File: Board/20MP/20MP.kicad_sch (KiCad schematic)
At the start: 48 parts, among them J1 Conn_01x02_Male, SW1 SHOU_HAN_MSK12C02-HB, SW2 RotaryEncoder_Switch, U1 nice_nanoV2

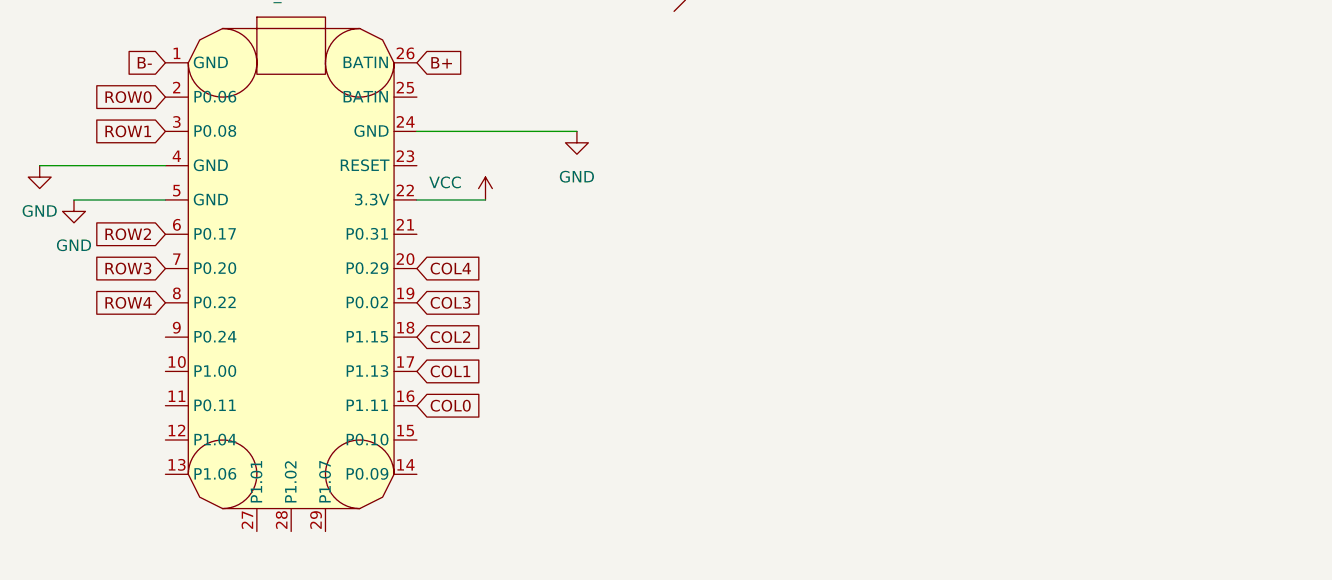
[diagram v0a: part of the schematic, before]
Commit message: added nice view to shematic
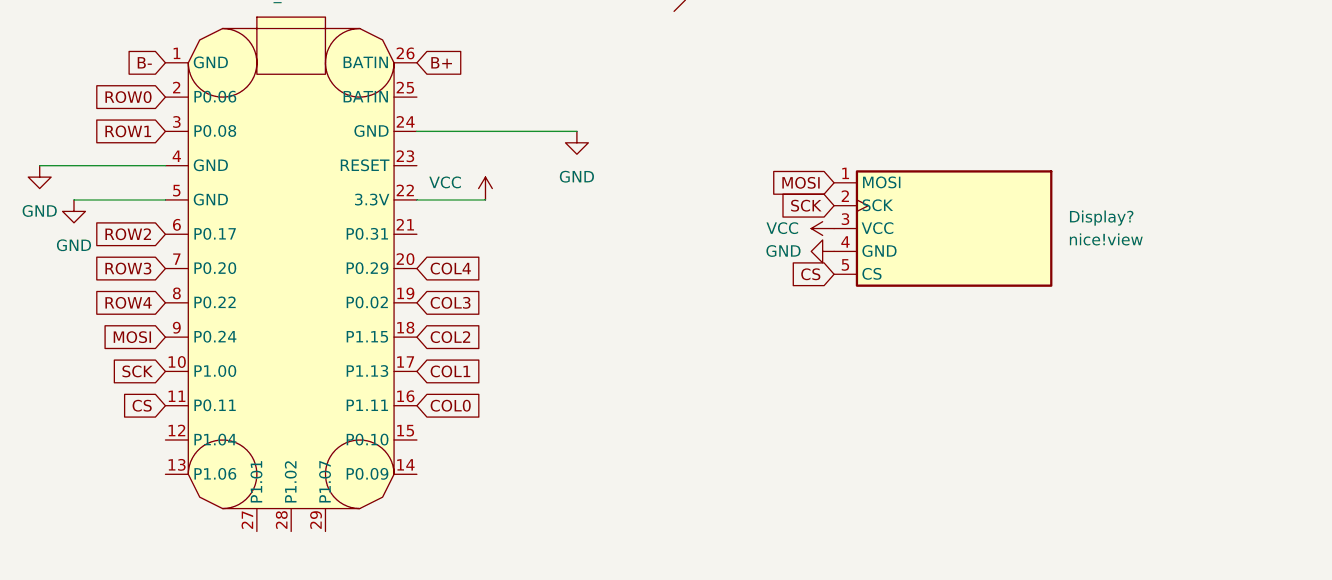
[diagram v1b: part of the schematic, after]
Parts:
- added Display?: nice!view, nice_view:nice_view, symbol microcontroller:nice!view
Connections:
- net GND: now also Display?.4 (GND)
- net VCC: now also Display?.3 (VCC)
- net SCK: now reaches U1.10 (P1.00)
- net SCK: now also Display?.2 (SCK)
- net CS: now reaches U1.11 (P0.11)
- net CS: now also Display?.5 (CS)
- net MOSI: now reaches U1.9 (P0.24)
- net MOSI: now also Display?.1 (MOSI)
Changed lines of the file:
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@@
+    )
+  )
+  (global_label "CS" (shape input) (at 63.5 105.41 180) (fields_autoplaced)
+    (effects (font (size 1.27 1.27)) (justify right))
+    (property "Intersheet References" "${INTERSHEET_REFS}" (id 0) (at 58.6074 105.3306 0)
+      (effects (font (size 1.27 1.27)) (justify right) hide)
+    )
+  )
+  (global_label "SCK" (shape input) (at 137.795 83.185 180) (fields_autoplaced)
+    (effects (font (size 1.27 1.27)) (justify right))
+    (property "Intersheet References" "${INTERSHEET_REFS}" (id 0) (at 131.6324 83.1056 0)
+      (effects (font (size 1.27 1.27)) (justify right) hide)
+    )
+  )
+  (global_label "SCK" (shape input) (at 63.5 101.6 180) (fields_autoplaced)
+    (effects (font (size 1.27 1.27)) (justify right))
+    (property "Intersheet References" "${INTERSHEET_REFS}" (id 0) (at 57.3374 101.5206 0)
+      (effects (font (size 1.27 1.27)) (justify right) hide)
     )
   )
@@
     )
   )
+  (global_label "MOSI" (shape input) (at 63.5 97.79 180) (fields_autoplaced)
+    (effects (font (size 1.27 1.27)) (justify right))
+    (property "Intersheet References" "${INTERSHEET_REFS}" (id 0) (at 56.4907 97.7106 0)
+      (effects (font (size 1.27 1.27)) (justify right) hide)
+    )
+  )
+  (global_label "MOSI" (shape input) (at 137.795 80.645 180) (fields_autoplaced)
+    (effects (font (size 1.27 1.27)) (justify right))
+    (property "Intersheet References" "${INTERSHEET_REFS}" (id 0) (at 130.7857 80.5656 0)
+      (effects (font (size 1.27 1.27)) (justify right) hide)
+    )
+  )
   (global_label "B+" (shape input) (at 112.395 52.705 180) (fields_autoplaced)
     (effects (font (size 1.27 1.27)) (justify right))
@@
     )
   )
+  (global_label "CS" (shape input) (at 137.795 90.805 180) (fields_autoplaced)
+    (effects (font (size 1.27 1.27)) (justify right))
+    (property "Intersheet References" "${INTERSHEET_REFS}" (id 0) (at 132.9024 90.7256 0)
+      (effects (font (size 1.27 1.27)) (justify right) hide)
+    )
+  )
   (global_label "B+" (shape input) (at 91.44 67.31 0) (fields_autoplaced)
     (effects (font (size 1.27 1.27)) (justify left))
@@
     (pin "1")
     (pin "2")
+  )
+  (symbol (lib_id "power:GND") (at 137.795 88.265 270) (unit 1)
+    (in_bom yes) (on_board yes)
+    (property "Reference" "#PWR?" (id 0) (at 131.445 88.265 0)
+      (effects (font (size 1.27 1.27)) hide)
+    )
+    (property "Value" "GND" (id 1) (at 130.175 88.265 90)
+      (effects (font (size 1.27 1.27)) (justify left))
+    )
+    (property "Footprint" "" (id 2) (at 137.795 88.265 0)
+      (effects (font (size 1.27 1.27)) hide)
+    )
+    (property "Datasheet" "" (id 3) (at 137.795 88.265 0)
+      (effects (font (size 1.27 1.27)) hide)
+    )
+    (pin "1")
   )
   (symbol (lib_id "led:D_Small") (at 267.335 151.765 90) (unit 1)
@@
     (pin "1")
     (pin "2")
+  )
+  (symbol (lib_id "power:VCC") (at 137.795 85.725 90) (unit 1)
+    (in_bom yes) (on_board yes)
+    (property "Reference" "#PWR?" (id 0) (at 141.605 85.725 0)
+      (effects (font (size 1.27 1.27)) hide)
+    )
+    (property "Value" "VCC" (id 1) (at 132.08 85.725 90))
+    (property "Footprint" "" (id 2) (at 137.795 85.725 0)
+      (effects (font (size 1.27 1.27)) hide)
+    )
+    (property "Datasheet" "" (id 3) (at 137.795 85.725 0)
+      (effects (font (size 1.27 1.27)) hide)
+    )
+    (pin "1")
   )
   (symbol (lib_id "pcb-rescue:MX-NoLED-MX_Alps_Hybrid") (at 220.345 145.415 0) (unit 1)
@@
     (pin "2")
   )
+  (symbol (lib_id "microcontroller:nice!view") (at 150.495 85.725 270) (unit 1)
+    (in_bom yes) (on_board yes) (fields_autoplaced)
+    (property "Reference" "Display?" (id 0) (at 163.83 84.4549 90)
+      (effects (font (size 1.27 1.27)) (justify left))
+    )
+    (property "Value" "nice!view" (id 1) (at 163.83 86.9949 90)
+      (effects (font (size 1.27 1.27)) (justify left))
+    )
+    (property "Footprint" "nice_view:nice_view" (id 2) (at 167.005 85.725 0)
+      (effects (font (size 1.27 1.27)) hide)
+    )
+    (property "Datasheet" "https://nicekeyboards.com/docs/nice-view/pinout-schematic" (id 3) (at 125.095 88.265 0)
+      (effects (font (size 1.27 1.27)) hide)
+    )
+    (pin "1")
+    (pin "2")
+    (pin "3")
+    (pin "4")
+    (pin "5")
+  )
   (symbol (lib_id "pcb-rescue:MX-NoLED-MX_Alps_Hybrid") (at 245.745 191.135 0) (unit 1)
     (in_bom yes) (on_board yes)
@@
       (reference "#PWR0107") (unit 1) (value "GND") (footprint "")
     )
+    (path "/077fa9e8-6ace-47c7-b2d9-a10ce67b4b2e"
+      (reference "#PWR?") (unit 1) (value "GND") (footprint "")
+    )
+    (path "/93480eee-d9fe-413d-9b83-523b8639fae5"
+      (reference "#PWR?") (unit 1) (value "VCC") (footprint "")
+    )
     (path "/737fc51a-35ee-45cc-8be4-9d28881bc01a"
       (reference "D1") (unit 1) (value "1.25V@150mA") (footprint "Diode_THT:D_DO-35_SOD27_P7.62mm_Horizontal")
@@
       (reference "D18") (unit 1) (value "1.25V@150mA") (footprint "Diode_THT:D_DO-35_SOD27_P7.62mm_Horizontal")
     )
+    (path "/fa417416-1aaa-4fd6-ba5d-3347f975a221"
+      (reference "Display?") (unit 1) (value "nice!view") (footprint "nice_view:nice_view")
+    )
     (path "/23241be8-f73f-4bb3-84de-fa8fd5f8d281"

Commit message: added nice view
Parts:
- Display1: renamed from Display?; footprint nice_view:nice_view -> microcontroller:nice_view
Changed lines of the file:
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@@
   (symbol (lib_id "power:GND") (at 137.795 88.265 270) (unit 1)
     (in_bom yes) (on_board yes)
-    (property "Reference" "#PWR?" (id 0) (at 131.445 88.265 0)
+    (property "Reference" "#PWR0101" (id 0) (at 131.445 88.265 0)
       (effects (font (size 1.27 1.27)) hide)
     )
@@
   (symbol (lib_id "power:VCC") (at 137.795 85.725 90) (unit 1)
     (in_bom yes) (on_board yes)
-    (property "Reference" "#PWR?" (id 0) (at 141.605 85.725 0)
+    (property "Reference" "#PWR0108" (id 0) (at 141.605 85.725 0)
       (effects (font (size 1.27 1.27)) hide)
     )
@@
   (symbol (lib_id "microcontroller:nice!view") (at 150.495 85.725 270) (unit 1)
     (in_bom yes) (on_board yes) (fields_autoplaced)
-    (property "Reference" "Display?" (id 0) (at 163.83 84.4549 90)
+    (property "Reference" "Display1" (id 0) (at 163.83 84.4549 90)
       (effects (font (size 1.27 1.27)) (justify left))
     )
@@
       (effects (font (size 1.27 1.27)) (justify left))
     )
-    (property "Footprint" "nice_view:nice_view" (id 2) (at 167.005 85.725 0)
+    (property "Footprint" "microcontroller:nice_view" (id 2) (at 167.005 85.725 0)
       (effects (font (size 1.27 1.27)) hide)
     )
@@
   )
   (symbol_instances
+    (path "/077fa9e8-6ace-47c7-b2d9-a10ce67b4b2e"
+      (reference "#PWR0101") (unit 1) (value "GND") (footprint "")
+    )
     (path "/1407de64-f7a0-4a9a-bd83-2447e7e8897c"
       (reference "#PWR0102") (unit 1) (value "GND") (footprint "")
@@
       (reference "#PWR0107") (unit 1) (value "GND") (footprint "")
     )
-    (path "/077fa9e8-6ace-47c7-b2d9-a10ce67b4b2e"
-      (reference "#PWR?") (unit 1) (value "GND") (footprint "")
-    )
     (path "/93480eee-d9fe-413d-9b83-523b8639fae5"
-      (reference "#PWR?") (unit 1) (value "VCC") (footprint "")
+      (reference "#PWR0108") (unit 1) (value "VCC") (footprint "")
     )
     (path "/737fc51a-35ee-45cc-8be4-9d28881bc01a"
@@
     )
     (path "/fa417416-1aaa-4fd6-ba5d-3347f975a221"
-      (reference "Display?") (unit 1) (value "nice!view") (footprint "nice_view:nice_view")
+      (reference "Display1") (unit 1) (value "nice!view") (footprint "microcontroller:nice_view")
     )
     (path "/23241be8-f73f-4bb3-84de-fa8fd5f8d281"

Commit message: changed diodes to smd
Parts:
- D1, D10, D11, D12, D13, D14, D15, D16, D17, D18, D2, D3, D4, D5, D6, D7, D8, D9: footprint Diode_THT:D_DO-35_SOD27_P7.62mm_Horizontal -> led:led_capacitor

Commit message: added matrix traces
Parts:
- D1, D10, D11, D12, D13, D14, D15, D16, D17, D18, D2, D3, D4, D5, D6, D7, D8, D9: footprint led:led_capacitor -> led:D_SOD-123
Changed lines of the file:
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@@
       (effects (font (size 1.27 1.27)) (justify right))
     )
-    (property "Footprint" "led:led_capacitor" (id 2) (at 216.535 187.325 90)
+    (property "Footprint" "led:D_SOD-123" (id 2) (at 216.535 187.325 90)
       (effects (font (size 1.27 1.27)) hide)
     )
@@
       (effects (font (size 1.27 1.27)) (justify right))
     )
-    (property "Footprint" "led:led_capacitor" (id 2) (at 267.335 141.605 90)
+    (property "Footprint" "led:D_SOD-123" (id 2) (at 267.335 141.605 90)
       (effects (font (size 1.27 1.27)) hide)
     )
@@
       (effects (font (size 1.27 1.27)) (justify right))
     )
-    (property "Footprint" "led:led_capacitor" (id 2) (at 216.535 167.005 90)
+    (property "Footprint" "led:D_SOD-123" (id 2) (at 216.535 167.005 90)
       (effects (font (size 1.27 1.27)) hide)
     )
@@
       (effects (font (size 1.27 1.27)) (justify right))
     )
-    (property "Footprint" "led:led_capacitor" (id 2) (at 314.96 177.8 90)
+    (property "Footprint" "led:D_SOD-123" (id 2) (at 314.96 177.8 90)
       (effects (font (size 1.27 1.27)) hide)
     )
@@
       (effects (font (size 1.27 1.27)) (justify right))
     )
-    (property "Footprint" "led:led_capacitor" (id 2) (at 267.335 167.005 90)
+    (property "Footprint" "led:D_SOD-123" (id 2) (at 267.335 167.005 90)
       (effects (font (size 1.27 1.27)) hide)
     )
@@
       (effects (font (size 1.27 1.27)) (justify right))
     )
-    (property "Footprint" "led:led_capacitor" (id 2) (at 267.335 116.205 90)
+    (property "Footprint" "led:D_SOD-123" (id 2) (at 267.335 116.205 90)
       (effects (font (size 1.27 1.27)) hide)
     )
@@
       (effects (font (size 1.27 1.27)) (justify right))
     )
-    (property "Footprint" "led:led_capacitor" (id 2) (at 216.535 141.605 90)
+    (property "Footprint" "led:D_SOD-123" (id 2) (at 216.535 141.605 90)
       (effects (font (size 1.27 1.27)) hide)
     )
@@
       (effects (font (size 1.27 1.27)) (justify right))
     )
-    (property "Footprint" "led:led_capacitor" (id 2) (at 241.935 141.605 90)
+    (property "Footprint" "led:D_SOD-123" (id 2) (at 241.935 141.605 90)
       (effects (font (size 1.27 1.27)) hide)
     )
@@
       (effects (font (size 1.27 1.27)) (justify right))
     )
-    (property "Footprint" "led:led_capacitor" (id 2) (at 216.535 90.805 90)
+    (property "Footprint" "led:D_SOD-123" (id 2) (at 216.535 90.805 90)
       (effects (font (size 1.27 1.27)) hide)
     )
@@
       (effects (font (size 1.27 1.27)) (justify right))
     )
-    (property "Footprint" "led:led_capacitor" (id 2) (at 292.735 116.205 90)
+    (property "Footprint" "led:D_SOD-123" (id 2) (at 292.735 116.205 90)
       (effects (font (size 1.27 1.27)) hide)
     )
@@
       (effects (font (size 1.27 1.27)) (justify right))
     )
-    (property "Footprint" "led:led_capacitor" (id 2) (at 216.535 116.205 90)
+    (property "Footprint" "led:D_SOD-123" (id 2) (at 216.535 116.205 90)
       (effects (font (size 1.27 1.27)) hide)
     )
@@
       (effects (font (size 1.27 1.27)) (justify right))
     )
-    (property "Footprint" "led:led_capacitor" (id 2) (at 241.935 167.005 90)
+    (property "Footprint" "led:D_SOD-123" (id 2) (at 241.935 167.005 90)
       (effects (font (size 1.27 1.27)) hide)
     )
@@
       (effects (font (size 1.27 1.27)) (justify right))
     )
-    (property "Footprint" "led:led_capacitor" (id 2) (at 241.935 90.805 90)
+    (property "Footprint" "led:D_SOD-123" (id 2) (at 241.935 90.805 90)
       (effects (font (size 1.27 1.27)) hide)
     )
@@
       (effects (font (size 1.27 1.27)) (justify right))
     )
-    (property "Footprint" "led:led_capacitor" (id 2) (at 241.935 187.325 90)
+    (property "Footprint" "led:D_SOD-123" (id 2) (at 241.935 187.325 90)
       (effects (font (size 1.27 1.27)) hide)
     )
@@
       (effects (font (size 1.27 1.27)) (justify right))
     )
-    (property "Footprint" "led:led_capacitor" (id 2) (at 292.735 90.805 90)
+    (property "Footprint" "led:D_SOD-123" (id 2) (at 292.735 90.805 90)
       (effects (font (size 1.27 1.27)) hide)
     )
@@
       (effects (font (size 1.27 1.27)) (justify right))
     )
-    (property "Footprint" "led:led_capacitor" (id 2) (at 292.735 141.605 90)
+    (property "Footprint" "led:D_SOD-123" (id 2) (at 292.735 141.605 90)
       (effects (font (size 1.27 1.27)) hide)
     )
@@
       (effects (font (size 1.27 1.27)) (justify right))
     )
-    (property "Footprint" "led:led_capacitor" (id 2) (at 267.335 90.805 90)
+    (property "Footprint" "led:D_SOD-123" (id 2) (at 267.335 90.805 90)
       (effects (font (size 1.27 1.27)) hide)
     )
@@
       (effects (font (size 1.27 1.27)) (justify right))
     )
-    (property "Footprint" "led:led_capacitor" (id 2) (at 241.935 116.205 90)
+    (property "Footprint" "led:D_SOD-123" (id 2) (at 241.935 116.205 90)
       (effects (font (size 1.27 1.27)) hide)
     )
@@
     )
     (path "/737fc51a-35ee-45cc-8be4-9d28881bc01a"
-      (reference "D1") (unit 1) (value "1.25V@150mA") (footprint "led:led_capacitor")
+      (reference "D1") (unit 1) (value "1.25V@150mA") (footprint "led:D_SOD-123")
     )
     (path "/828cf1c3-df22-4977-bdc4-6d4dc39f11a6"
-      (reference "D2") (unit 1) (value "1.25V@150mA") (footprint "led:led_capacitor")
+      (reference "D2") (unit 1) (value "1.25V@150mA") (footprint "led:D_SOD-123")
     )
     (path "/70d2644a-7097-4af7-a972-803c0d643478"
-      (reference "D3") (unit 1) (value "1.25V@150mA") (footprint "led:led_capacitor")
+      (reference "D3") (unit 1) (value "1.25V@150mA") (footprint "led:D_SOD-123")
     )
     (path "/249d342e-814c-4657-b87f-4a948cf09f83"
-      (reference "D4") (unit 1) (value "1.25V@150mA") (footprint "led:led_capacitor")
+      (reference "D4") (unit 1) (value "1.25V@150mA") (footprint "led:D_SOD-123")
     )
     (path "/0142f8b5-c800-43db-9d31-5f9eb56a3541"
-      (reference "D5") (unit 1) (value "1.25V@150mA") (footprint "led:led_capacitor")
+      (reference "D5") (unit 1) (value "1.25V@150mA") (footprint "led:D_SOD-123")
     )
     (path "/ba13f5a9-b55a-43bb-9158-6065ece3054a"
-      (reference "D6") (unit 1) (value "1.25V@150mA") (footprint "led:led_capacitor")
+      (reference "D6") (unit 1) (value "1.25V@150mA") (footprint "led:D_SOD-123")
     )
     (path "/f52a7792-b2ba-41b3-b87f-915a0d15a464"
-      (reference "D7") (unit 1) (value "1.25V@150mA") (footprint "led:led_capacitor")
+      (reference "D7") (unit 1) (value "1.25V@150mA") (footprint "led:D_SOD-123")
     )
     (path "/733cc8ef-d71d-4b0e-b748-90c3ff173b3e"
-      (reference "D8") (unit 1) (value "1.25V@150mA") (footprint "led:led_capacitor")
+      (reference "D8") (unit 1) (value "1.25V@150mA") (footprint "led:D_SOD-123")
     )
     (path "/ac5ab474-27f7-4252-9f2e-0a1481cf7f98"
-      (reference "D9") (unit 1) (value "1.25V@150mA") (footprint "led:led_capacitor")
+      (reference "D9") (unit 1) (value "1.25V@150mA") (footprint "led:D_SOD-123")
     )
     (path "/c14c0489-ba57-4809-b1ce-5b757b133c92"
-      (reference "D10") (unit 1) (value "1.25V@150mA") (footprint "led:led_capacitor")
+      (reference "D10") (unit 1) (value "1.25V@150mA") (footprint "led:D_SOD-123")
     )
     (path "/ee591613-253d-445b-b2ba-194a6782e1b3"
-      (reference "D11") (unit 1) (value "1.25V@150mA") (footprint "led:led_capacitor")
+      (reference "D11") (unit 1) (value "1.25V@150mA") (footprint "led:D_SOD-123")
     )
     (path "/68ef6fcf-ede0-4658-b0d5-8555f9ef1de8"
-      (reference "D12") (unit 1) (value "1.25V@150mA") (footprint "led:led_capacitor")
+      (reference "D12") (unit 1) (value "1.25V@150mA") (footprint "led:D_SOD-123")
     )
     (path "/118543a5-4101-486e-96d3-1d1e2c3ef475"
-      (reference "D13") (unit 1) (value "1.25V@150mA") (footprint "led:led_capacitor")
+      (reference "D13") (unit 1) (value "1.25V@150mA") (footprint "led:D_SOD-123")
     )
     (path "/61ef8754-e7e5-4d00-bf69-9cc99d774223"
-      (reference "D14") (unit 1) (value "1.25V@150mA") (footprint "led:led_capacitor")
+      (reference "D14") (unit 1) (value "1.25V@150mA") (footprint "led:D_SOD-123")
     )
     (path "/c491c0d6-bf46-4014-961a-eeda9d2042f5"
-      (reference "D15") (unit 1) (value "1.25V@150mA") (footprint "led:led_capacitor")
+      (reference "D15") (unit 1) (value "1.25V@150mA") (footprint "led:D_SOD-123")
     )
     (path "/774f43fa-8de8-4aa5-b190-f426ed72b9ef"
-      (reference "D16") (unit 1) (value "1.25V@150mA") (footprint "led:led_capacitor")
+      (reference "D16") (unit 1) (value "1.25V@150mA") (footprint "led:D_SOD-123")
     )
     (path "/e2f7c2f2-3149-4b68-9543-0f142d79f479"
-      (reference "D17") (unit 1) (value "1.25V@150mA") (footprint "led:led_capacitor")
+      (reference "D17") (unit 1) (value "1.25V@150mA") (footprint "led:D_SOD-123")
     )
     (path "/4a34ca48-2763-4753-90a4-ef0bab121257"
-      (reference "D18") (unit 1) (value "1.25V@150mA") (footprint "led:led_capacitor")
+      (reference "D18") (unit 1) (value "1.25V@150mA") (footprint "led:D_SOD-123")
     )
     (path "/fa417416-1aaa-4fd6-ba5d-3347f975a221"
